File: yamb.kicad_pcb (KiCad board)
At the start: 2 copper layers, 9 parts, among them J1 Barrel_Jack, J2 I2C, J3 HEADER, J4 HEADER_2.54, P1 USB_C_Plug_USB2.0, U1 TPS3808DBV

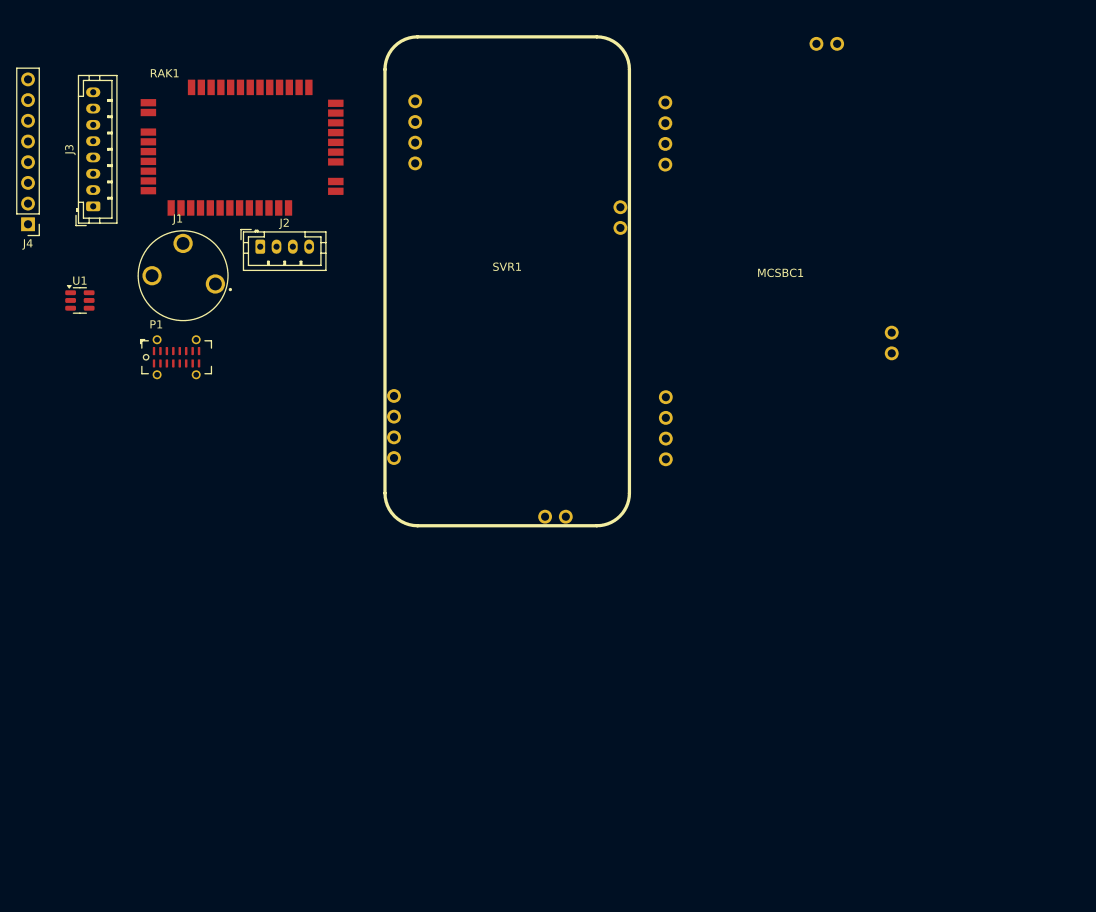
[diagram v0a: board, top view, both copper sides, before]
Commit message: additional footprints for reset, power switch, correct USB-C symbol for footprint, bypass jumpers for watchdog and pwr switch
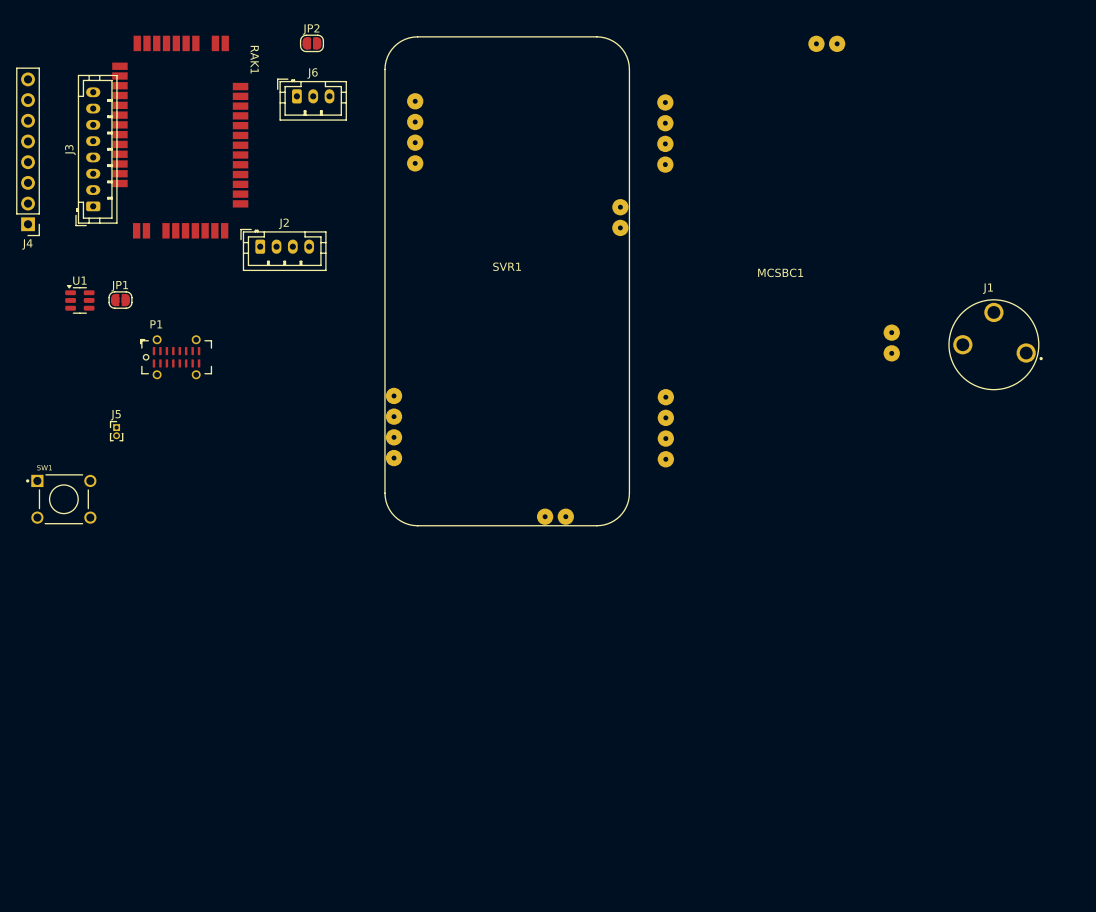
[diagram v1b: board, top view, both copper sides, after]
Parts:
- added J5: Remote_Reset, Connector_PinHeader_1.00mm:PinHeader_1x02_P1.00mm_Vertical, F.Cu at (60.9, 63.1)
- added J6: Power_Switch, Connector_JST:JST_PH_B3B-PH-K_1x03_P2.00mm_Vertical, F.Cu at (83.0, 22.5)
- added JP1: WATCHDOG_ENABLE, Jumper:SolderJumper-2_P1.3mm_Open_RoundedPad1.0x1.5mm, F.Cu at (61.4, 47.5)
- added JP2: PWR_SW_BYPASS, Jumper:SolderJumper-2_P1.3mm_Open_RoundedPad1.0x1.5mm, F.Cu at (84.8, 16.0)
- added SW1: RESET, Button_Switch_THT:SW_1825910-6-4, F.Cu at (54.4, 72.0)
- moved J1 99.9 mm to (168.5, 53.0)
- moved RAK1 6.49 mm to (69.8, 27.5), turned to -90 degrees
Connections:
- J1 pad PIN: (no net) -> 7-20V
- J1 pad SLV: (no net) -> GND
- J1 pad S_S: (no net) -> unconnected-(J1-PadS_S)
- MCSBC1 pad 11: +3.3V -> PWR_SW
- MCSBC1 pad 9: +3.3V -> PWR_SW
- P1 pad A8: (no net) -> unconnected-(P1-SBU1-PadA8)
- P1 pad B6: (no net) -> unconnected-(P1-D+-PadB6)
- P1 pad B7: (no net) -> unconnected-(P1-D--PadB7)
- P1 pad B8: (no net) -> unconnected-(P1-SBU2-PadB8)
- SVR1 pad 10: (no net) -> GND
- SVR1 pad 11: (no net) -> GND
- SVR1 pad 12: +3.3V -> THRU
- SVR1 pad 6: (no net) -> GND
- SVR1 pad 8: GND -> 7-20V
- SVR1 pad 9: VIN -> PWR_SW
- U1 pad 6: VBUS -> Net-(JP1-B)

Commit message: custom libraries
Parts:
- removed MCSBC1: U2, Converter_DCDC:Voltaic_MCSBC
- removed RAK1: U4, RF_Module:RAK4630
- removed SVR1: U3, Converter_DCDC:Voltaic_SVR
- added U2: MCSBC, Andy_Footprints:Voltaic_MCSBC, F.Cu at (129.0, 14.5)
- added U3: SVR, Andy_Footprints:Voltaic_SVR, F.Cu at (126.5, 76.5)
- added U4: RAK4630, Andy_Footprints:RAK4630, F.Cu at (72.0, 26.5)
- J3: footprint Connector_JST:JST_PH_B8B-PH-K_1x08_P2.00mm_Vertical -> Connector_JST:JST_PHD_B16B-PHDSS_2x08_P2.00mm_Vertical
- J4: footprint Connector_PinHeader_2.54mm:PinHeader_1x08_P2.54mm_Vertical -> Connector_PinHeader_2.54mm:PinHeader_2x08_P2.54mm_Vertical
- moved J1 83.7 mm to (86.5, 69.5)
- moved SW1 38.2 mm to (87.8, 53.2)
- moved P1 26.8 mm to (86.5, 34.9), turned to 90 degrees
- moved J4 20.1 mm to (61.0, 55.0), turned to 90 degrees
- moved J5 13.2 mm to (57.0, 50.5)
- moved J3 10.4 mm to (64.0, 44.5), turned to 0 degrees
- moved U1 8.73 mm to (58.4, 39.0)
- moved J2 7.24 mm to (84.5, 45.0)
- moved JP1 4.84 mm to (58.0, 44.0)
- moved J6 2.50 mm to (85.5, 22.5)
- moved JP2 2.50 mm to (87.3, 16.0)
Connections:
- J1 pad PIN: 7-20V -> (no net)
- J1 pad SLV: GND -> (no net)
- J1 pad S_S: unconnected-(J1-PadS_S) -> (no net)
- J2 pad 3: 3V3_I2C -> 3V3
- J3 pad 1: +5V -> +3.3V
- J3 pad 2: SW2 -> unconnected-(J3-Pin_2-Pad2)
- J3 pad 3: SW1 -> SW2
- J3 pad 4: LED2 -> unconnected-(J3-Pin_4-Pad4)
- J3 pad 5: LED1 -> SW1
- J3 pad 6: AIN3 -> unconnected-(J3-Pin_6-Pad6)
- J3 pad 7: AIN2 -> LED2
- J3 pad 8: GND -> unconnected-(J3-Pin_8-Pad8)
- J4 pad 1: +5V -> +3.3V
- J4 pad 2: SW2 -> unconnected-(J4-Pin_2-Pad2)
- J4 pad 3: SW1 -> SW2
- J4 pad 4: LED2 -> unconnected-(J4-Pin_4-Pad4)
- J4 pad 5: LED1 -> SW1
- J4 pad 6: AIN3 -> unconnected-(J4-Pin_6-Pad6)
- J4 pad 7: AIN2 -> LED2
- J4 pad 8: GND -> unconnected-(J4-Pin_8-Pad8)
- P1 pad A4: +5V -> VBUS
- P1 pad A9: +5V -> VBUS
- P1 pad B4: +5V -> VBUS
- P1 pad B9: +5V -> VBUS
- SW1 pad 3: (no net) -> unconnected-(SW1-Pad3)
- SW1 pad 4: (no net) -> unconnected-(SW1-Pad4)

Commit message: solving ERC errors
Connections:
- J1 pad PIN: (no net) -> 7-20V
- J1 pad SLV: (no net) -> GND
- J1 pad S_S: (no net) -> unconnected-(J1-PadS_S)
- J3 pad 2: unconnected-(J3-Pin_2-Pad2) -> UART_TX
- J3 pad 4: unconnected-(J3-Pin_4-Pad4) -> UAART_RX
- J4 pad 2: unconnected-(J4-Pin_2-Pad2) -> UART_TX
- J4 pad 4: unconnected-(J4-Pin_4-Pad4) -> UAART_RX
- J6 pad 3: PWR_SW -> 3V3
- JP2 pad 2: PWR_SW -> 3V3
- U2 pad 1: BATT -> +BATT
- U3 pad 5: BATT -> +BATT
- U3 pad 9: PWR_SW -> +3.3V
- U4 pad 10: unconnected-(U4-UART1_TX-Pad10) -> UART_TX
- U4 pad 44: unconnected-(U4-VBAT_NRF-Pad44) -> +BATT
- U4 pad 9: unconnected-(U4-UART1_RX-Pad9) -> UAART_RX

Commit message: PCB layout first pass
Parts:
- moved JP1 115.5 mm to (156.2, 104.8), turned to 90 degrees
- moved U1 114.0 mm to (156.1, 97.8)
- moved JP2 108.6 mm to (149.9, 104.8), turned to 90 degrees
- moved J5 103.9 mm to (149.9, 97.0)
- moved J3 102.7 mm to (155.7, 90.9), turned to 180 degrees
- moved J4 100.0 mm to (157.5, 81.3), turned to -90 degrees
- moved J6 98.8 mm to (140.1, 104.8)
- moved J1 83.1 mm to (167.6, 87.6), turned to 180 degrees
- moved U4 81.9 mm to (121.9, 91.4), turned to 180 degrees
- moved P1 75.9 mm to (115.5, 105.0), turned to 0 degrees
- moved J2 73.1 mm to (126.5, 104.8)
- moved SW1 70.4 mm to (142.2, 97.8)
- moved U3 63.7 mm to (141.3, 14.5), turned to 0 degrees
- moved U2 63.2 mm to (141.0, 76.5), turned to 180 degrees
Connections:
- J3 pad 3: SW2 -> LED2
- J3 pad 5: SW1 -> LED1
- J3 pad 7: LED2 -> SW2
- J3 pad 9: LED1 -> SW1
- J4 pad 3: SW2 -> LED2
- J4 pad 5: SW1 -> LED1
- J4 pad 7: LED2 -> SW2
- J4 pad 9: LED1 -> SW1
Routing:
- net +3.3V: track 0.00 -> 124.7 mm, vias 0 -> 2
- net +BATT: track 0.00 -> 120.9 mm
- net SDA: track 0.00 -> 100.1 mm, vias 0 -> 1
- net 3V3: track 0.00 -> 98.2 mm
- net SCL: track 0.00 -> 97.7 mm, vias 0 -> 1
- net AIN3: track 0.00 -> 51.3 mm
- net AIN2: track 0.00 -> 49.2 mm
- net LED2: track 0.00 -> 45.7 mm
- net UART_TX: track 0.00 -> 42.1 mm
- net LED1: track 0.00 -> 41.4 mm
- net UAART_RX: track 0.00 -> 41.1 mm
- net SW2: track 0.00 -> 37.3 mm
- net 7-20V: track 0.00 -> 36.3 mm
- net SW1: track 0.00 -> 33.3 mm
- net RESET: track 0.00 -> 24.2 mm, vias 0 -> 2
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- added copper zone on B.Cu, net GND
- added copper zone on F.Cu, net GND
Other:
- board outline added: 67.7 x 96.7 mm

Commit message: some board layout stuff
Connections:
- J3 pad 1: +3.3V -> 3V3
- J4 pad 1: +3.3V -> 3V3
- JP1 pad 1: +3.3V -> 3V3
- U1 pad 5: +3.3V -> 3V3
- U4 pad 20: +3.3V -> 3V3
- U4 pad 21: +3.3V -> 3V3
- U4 pad 43: +3.3V -> 3V3

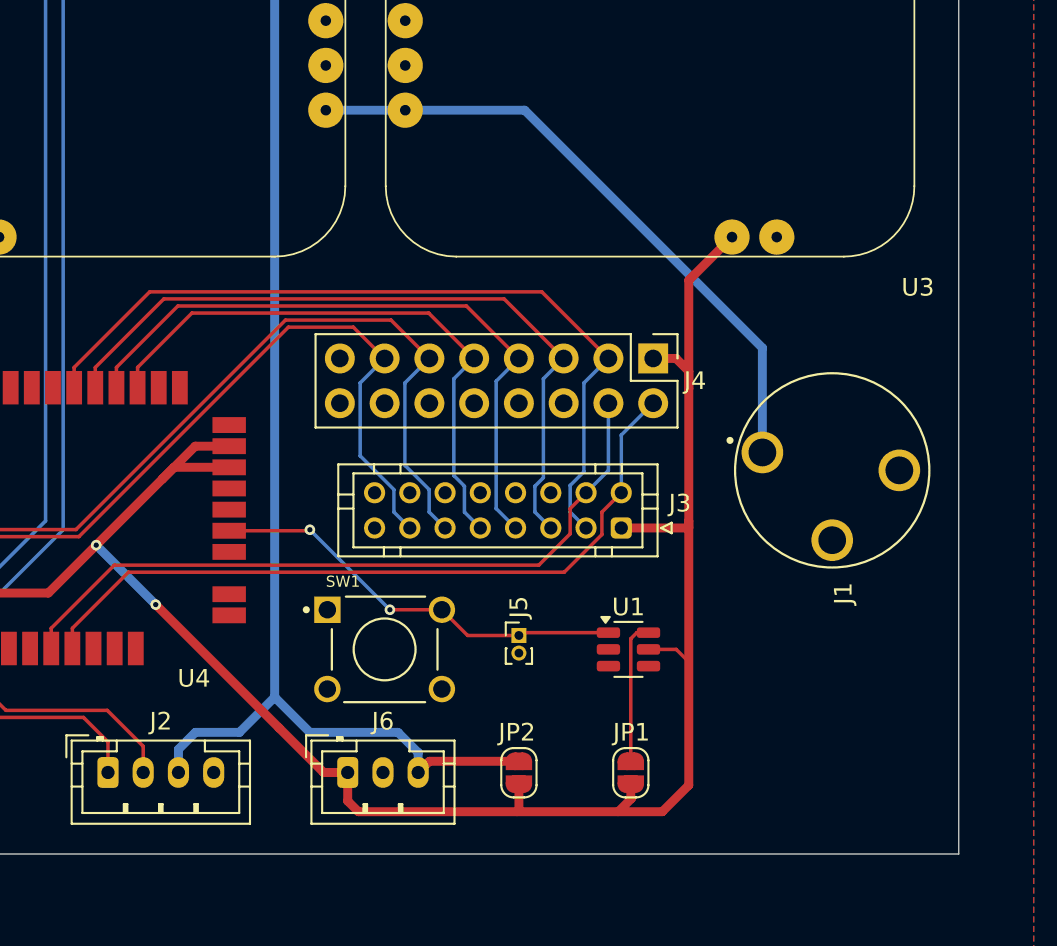
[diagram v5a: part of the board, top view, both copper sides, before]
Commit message: some 3D components, adding BME280, some 3V3 vs 3.3V fixes
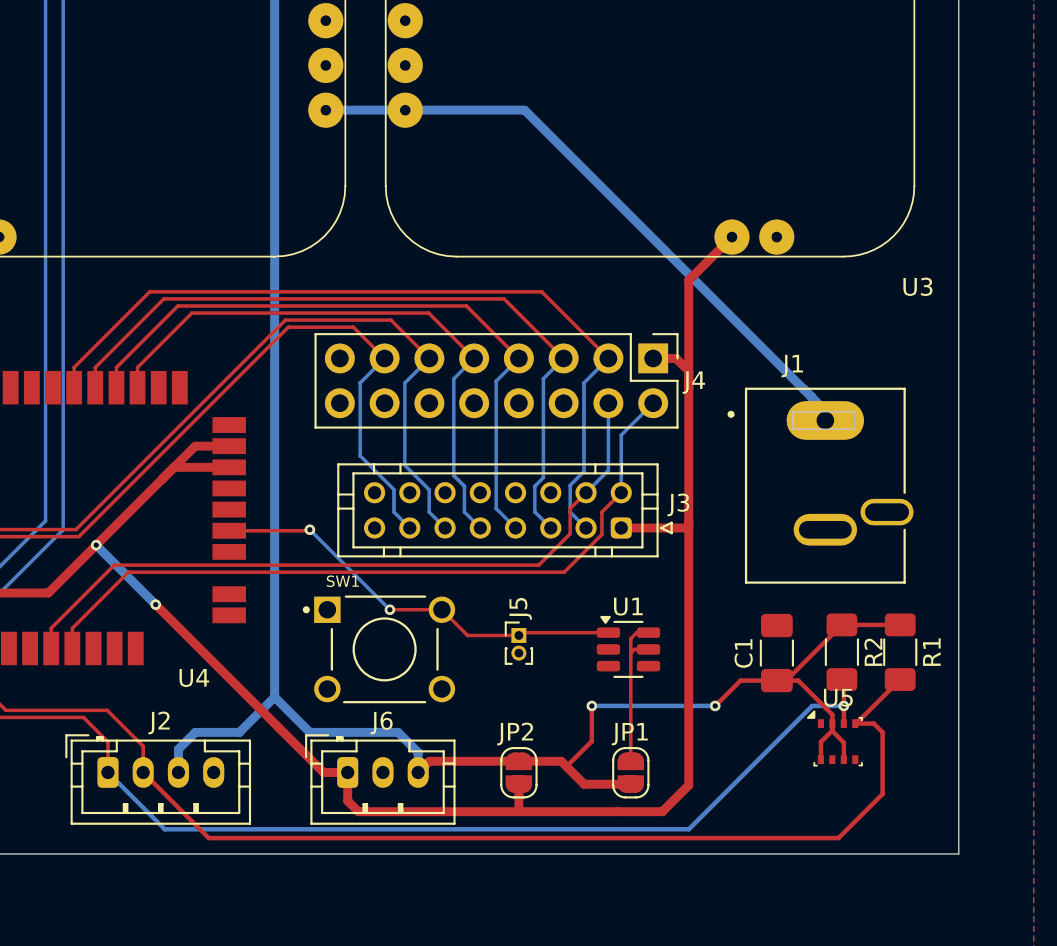
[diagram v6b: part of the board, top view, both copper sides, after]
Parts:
- added C1: BMECAP, Capacitor_SMD:C_1206_3216Metric_Pad1.33x1.80mm_HandSolder, F.Cu at (164.5, 98.0)
- added R1: R, Resistor_SMD:R_1206_3216Metric_Pad1.30x1.75mm_HandSolder, F.Cu at (171.5, 98.0)
- added R2: R, Resistor_SMD:R_1206_3216Metric_Pad1.30x1.75mm_HandSolder, F.Cu at (168.2, 98.0)
- added U5: BME280, Package_LGA:Bosch_LGA-8_2.5x2.5mm_P0.65mm_ClockwisePinNumbering, F.Cu at (168.0, 103.0)
- J1: footprint Connector_BarrelJack:SWITCHCRAFT_PC722A -> Andy_Footprints:CUI_PJ-044A
- moved J1 0.95 mm to (167.2, 88.5), turned to 0 degrees
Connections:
- JP1 pad 2: Net-(JP1-B) -> WATCHDOGVDD
- U1 pad 5: 3V3 -> WATCHDOGVDD
- U1 pad 6: Net-(JP1-B) -> WATCHDOGVDD
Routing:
- net SCL: track 97.7 -> 151.1 mm
- net SDA: track 100.1 -> 148.7 mm, vias 1 -> 2
- net 3V3: track 98.2 -> 137.6 mm, vias 0 -> 2
- net WATCHDOGVDD: track 0.00 -> 9.20 mm
- net Net-(JP1-B): track 8.10 -> 0.00 mm
- net +3.3V: track 124.7 -> 120.3 mm
